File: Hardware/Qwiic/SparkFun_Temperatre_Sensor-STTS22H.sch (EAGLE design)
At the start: 28 parts, among them J1 QWIIC_RIGHT_ANGLE, J2 QWIIC_RIGHT_ANGLE, U2 STTS22H

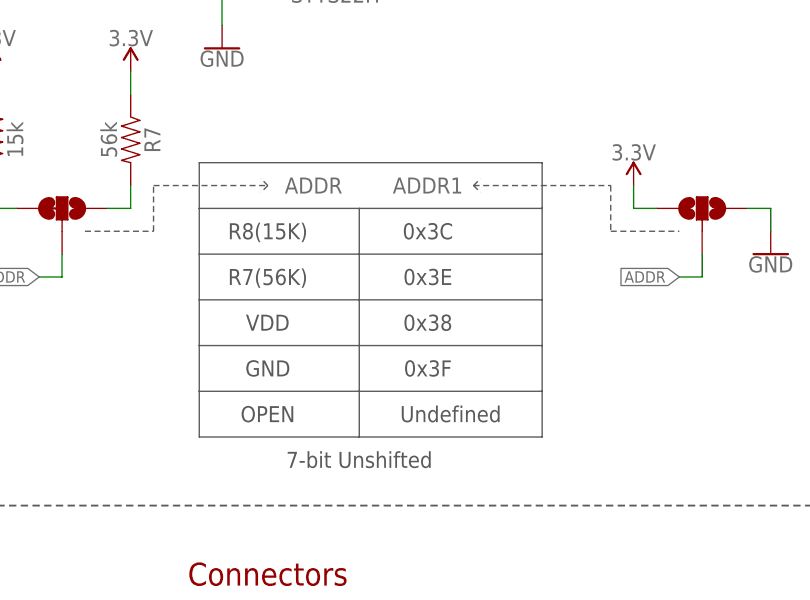
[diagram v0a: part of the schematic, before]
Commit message: Adds note for default addresses
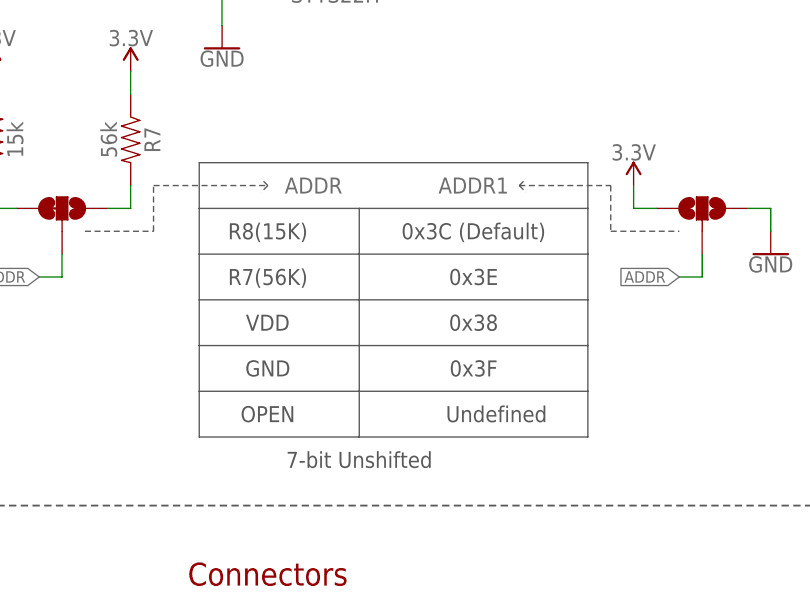
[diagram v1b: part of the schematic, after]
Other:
- note added: "0x3C (Default)"
- note removed: "0x3C"
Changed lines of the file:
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@@
 <wire x1="40.64" y1="86.36" x2="40.64" y2="81.28" width="0.1524" layer="97"/>
 <wire x1="40.64" y1="81.28" x2="40.64" y2="76.2" width="0.1524" layer="97"/>
-<wire x1="58.42" y1="76.2" x2="78.74" y2="76.2" width="0.1524" layer="97"/>
-<wire x1="78.74" y1="76.2" x2="78.74" y2="81.28" width="0.1524" layer="97"/>
-<wire x1="78.74" y1="81.28" x2="78.74" y2="86.36" width="0.1524" layer="97"/>
-<wire x1="78.74" y1="86.36" x2="78.74" y2="91.44" width="0.1524" layer="97"/>
-<wire x1="78.74" y1="91.44" x2="78.74" y2="96.52" width="0.1524" layer="97"/>
-<wire x1="78.74" y1="96.52" x2="78.74" y2="101.6" width="0.1524" layer="97"/>
-<wire x1="78.74" y1="101.6" x2="78.74" y2="106.68" width="0.1524" layer="97"/>
-<wire x1="78.74" y1="106.68" x2="40.64" y2="106.68" width="0.1524" layer="97"/>
+<wire x1="58.42" y1="76.2" x2="83.82" y2="76.2" width="0.1524" layer="97"/>
+<wire x1="83.82" y1="76.2" x2="83.82" y2="81.28" width="0.1524" layer="97"/>
+<wire x1="83.82" y1="81.28" x2="83.82" y2="86.36" width="0.1524" layer="97"/>
+<wire x1="83.82" y1="86.36" x2="83.82" y2="91.44" width="0.1524" layer="97"/>
+<wire x1="83.82" y1="91.44" x2="83.82" y2="96.52" width="0.1524" layer="97"/>
+<wire x1="83.82" y1="96.52" x2="83.82" y2="101.6" width="0.1524" layer="97"/>
+<wire x1="83.82" y1="101.6" x2="83.82" y2="106.68" width="0.1524" layer="97"/>
+<wire x1="83.82" y1="106.68" x2="40.64" y2="106.68" width="0.1524" layer="97"/>
 <wire x1="40.64" y1="101.6" x2="58.42" y2="101.6" width="0.1524" layer="97"/>
-<wire x1="58.42" y1="101.6" x2="78.74" y2="101.6" width="0.1524" layer="97"/>
+<wire x1="58.42" y1="101.6" x2="83.82" y2="101.6" width="0.1524" layer="97"/>
 <wire x1="58.42" y1="101.6" x2="58.42" y2="96.52" width="0.1524" layer="97"/>
 <wire x1="58.42" y1="96.52" x2="58.42" y2="91.44" width="0.1524" layer="97"/>
@@
 <wire x1="40.64" y1="81.28" x2="58.42" y2="81.28" width="0.1524" layer="97"/>
 <wire x1="40.64" y1="76.2" x2="58.42" y2="76.2" width="0.1524" layer="97"/>
-<wire x1="58.42" y1="96.52" x2="78.74" y2="96.52" width="0.1524" layer="97"/>
-<wire x1="58.42" y1="81.28" x2="78.74" y2="81.28" width="0.1524" layer="97"/>
+<wire x1="58.42" y1="96.52" x2="83.82" y2="96.52" width="0.1524" layer="97"/>
+<wire x1="58.42" y1="81.28" x2="83.82" y2="81.28" width="0.1524" layer="97"/>
 <text x="48.26" y="88.9" size="1.778" layer="97" font="vector" align="center">VDD</text>
 <text x="48.26" y="83.82" size="1.778" layer="97" font="vector" align="center">GND</text>
 <text x="48.26" y="78.74" size="1.778" layer="97" font="vector" align="center">OPEN</text>
-<text x="68.58" y="78.74" size="1.778" layer="97" font="vector" align="center">Undefined</text>
+<text x="73.66" y="78.74" size="1.778" layer="97" font="vector" align="center">Undefined</text>
 <text x="58.42" y="73.66" size="1.778" layer="97" font="vector" align="center">7-bit Unshifted</text>
 <wire x1="40.64" y1="91.44" x2="58.42" y2="91.44" width="0.1524" layer="97"/>
-<wire x1="58.42" y1="91.44" x2="78.74" y2="91.44" width="0.1524" layer="97"/>
+<wire x1="58.42" y1="91.44" x2="83.82" y2="91.44" width="0.1524" layer="97"/>
 <wire x1="40.64" y1="86.36" x2="58.42" y2="86.36" width="0.1524" layer="97"/>
-<wire x1="58.42" y1="86.36" x2="78.74" y2="86.36" width="0.1524" layer="97"/>
+<wire x1="58.42" y1="86.36" x2="83.82" y2="86.36" width="0.1524" layer="97"/>
 <text x="48.26" y="93.98" size="1.778" layer="97" font="vector" align="center">R7(56K)</text>
 <text x="48.26" y="99.06" size="1.778" layer="97" font="vector" align="center">R8(15K)</text>
-<text x="66.04" y="88.9" size="1.778" layer="97" font="vector" align="center">0x38</text>
-<text x="66.04" y="99.06" size="1.778" layer="97" font="vector" align="center">0x3C</text>
-<text x="66.04" y="93.98" size="1.778" layer="97" font="vector" align="center">0x3E</text>
-<text x="66.04" y="83.82" size="1.778" layer="97" font="vector" align="center">0x3F</text>
+<text x="71.12" y="88.9" size="1.778" layer="97" font="vector" align="center">0x38</text>
+<text x="71.12" y="99.06" size="1.778" layer="97" font="vector" align="center">0x3C (Default)</text>
+<text x="71.12" y="93.98" size="1.778" layer="97" font="vector" align="center">0x3E</text>
+<text x="71.12" y="83.82" size="1.778" layer="97" font="vector" align="center">0x3F</text>
 <wire x1="27.94" y1="99.06" x2="35.56" y2="99.06" width="0.1524" layer="97" style="dashdot"/>
 <wire x1="35.56" y1="99.06" x2="35.56" y2="104.14" width="0.1524" layer="97" style="dashdot"/>
 <wire x1="35.56" y1="104.14" x2="48.26" y2="104.14" width="0.1524" layer="97" style="dashdot"/>
-<wire x1="71.12" y1="104.14" x2="86.36" y2="104.14" width="0.1524" layer="97" style="dashdot"/>
+<wire x1="76.2" y1="104.14" x2="86.36" y2="104.14" width="0.1524" layer="97" style="dashdot"/>
 <wire x1="86.36" y1="104.14" x2="86.36" y2="99.06" width="0.1524" layer="97" style="dashdot"/>
 <wire x1="86.36" y1="99.06" x2="93.98" y2="99.06" width="0.1524" layer="97" style="dashdot"/>
 <wire x1="48.26" y1="104.14" x2="47.498" y2="104.902" width="0.1524" layer="97" style="dashdot"/>
 <wire x1="48.26" y1="104.14" x2="47.498" y2="103.378" width="0.1524" layer="97" style="dashdot"/>
-<wire x1="71.12" y1="104.14" x2="71.882" y2="104.902" width="0.1524" layer="97" style="dashdot"/>
-<wire x1="71.12" y1="104.14" x2="71.882" y2="103.378" width="0.1524" layer="97" style="dashdot"/>
+<wire x1="76.2" y1="104.14" x2="76.962" y2="104.902" width="0.1524" layer="97" style="dashdot"/>
+<wire x1="76.2" y1="104.14" x2="76.962" y2="103.378" width="0.1524" layer="97" style="dashdot"/>
 <text x="58.42" y="175.26" size="2.54" layer="94" font="vector" align="center">Temperature Sensor - STTS22H</text>
 </plain>
@@
 </instance>
 <instance part="ADDR1" gate="G$1" x="96.52" y="101.6" smashed="yes" rot="MR90">
-<attribute name="NAME" x="66.04" y="104.14" size="1.778" layer="95" font="vector" rot="MR0" align="center"/>
+<attribute name="NAME" x="71.12" y="104.14" size="1.778" layer="95" font="vector" rot="MR0" align="center"/>
 </instance>
 <instance part="SUPPLY8" gate="G$1" x="88.9" y="104.14" smashed="yes">

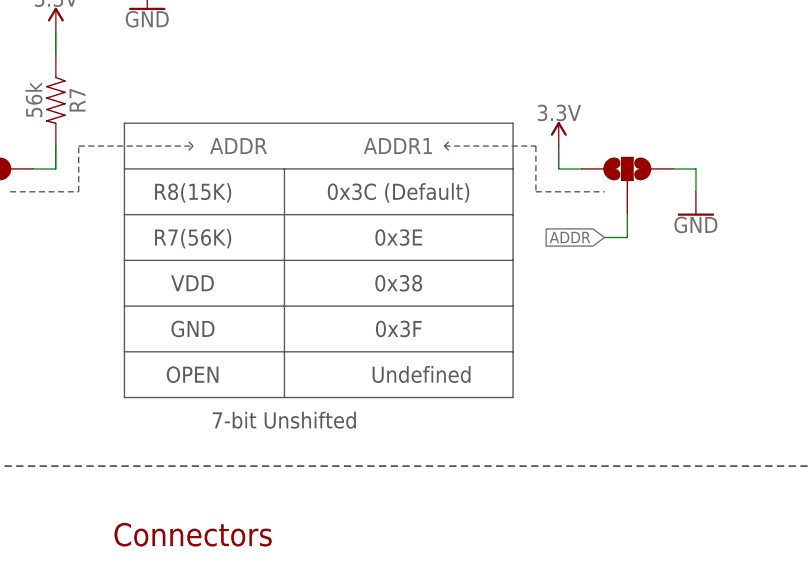
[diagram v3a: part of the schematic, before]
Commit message: Updates temp sensor footprint, Adds bstop underneath IC
* Adds via directly underneath sensor for better temperature sensing
* Fixes various routing inconsistencies
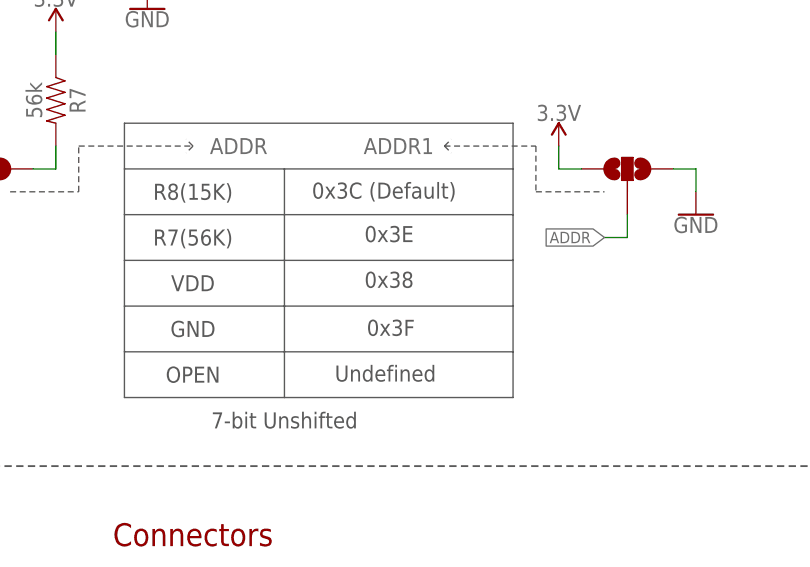
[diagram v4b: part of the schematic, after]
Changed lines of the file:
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@@
 <text x="48.26" y="83.82" size="1.778" layer="97" font="vector" align="center">GND</text>
 <text x="48.26" y="78.74" size="1.778" layer="97" font="vector" align="center">OPEN</text>
-<text x="73.66" y="78.74" size="1.778" layer="97" font="vector" align="center">Undefined</text>
+<text x="64.008" y="77.978" size="1.778" layer="97" font="vector">Undefined</text>
 <text x="58.42" y="73.66" size="1.778" layer="97" font="vector" align="center">7-bit Unshifted</text>
 <wire x1="40.64" y1="91.44" x2="58.42" y2="91.44" width="0.1524" layer="97"/>
@@
 <text x="48.26" y="93.98" size="1.778" layer="97" font="vector" align="center">R7(56K)</text>
 <text x="48.26" y="99.06" size="1.778" layer="97" font="vector" align="center">R8(15K)</text>
-<text x="71.12" y="88.9" size="1.778" layer="97" font="vector" align="center">0x38</text>
-<text x="71.12" y="99.06" size="1.778" layer="97" font="vector" align="center">0x3C (Default)</text>
-<text x="71.12" y="93.98" size="1.778" layer="97" font="vector" align="center">0x3E</text>
-<text x="71.12" y="83.82" size="1.778" layer="97" font="vector" align="center">0x3F</text>
+<text x="67.31" y="88.392" size="1.778" layer="97" font="vector">0x38</text>
+<text x="61.468" y="98.298" size="1.778" layer="97" font="vector" ratio="15">0x3C (Default)</text>
+<text x="67.31" y="93.472" size="1.778" layer="97" font="vector">0x3E</text>
+<text x="67.564" y="83.058" size="1.778" layer="97" font="vector">0x3F</text>
 <wire x1="27.94" y1="99.06" x2="35.56" y2="99.06" width="0.1524" layer="97" style="dashdot"/>
 <wire x1="35.56" y1="99.06" x2="35.56" y2="104.14" width="0.1524" layer="97" style="dashdot"/>

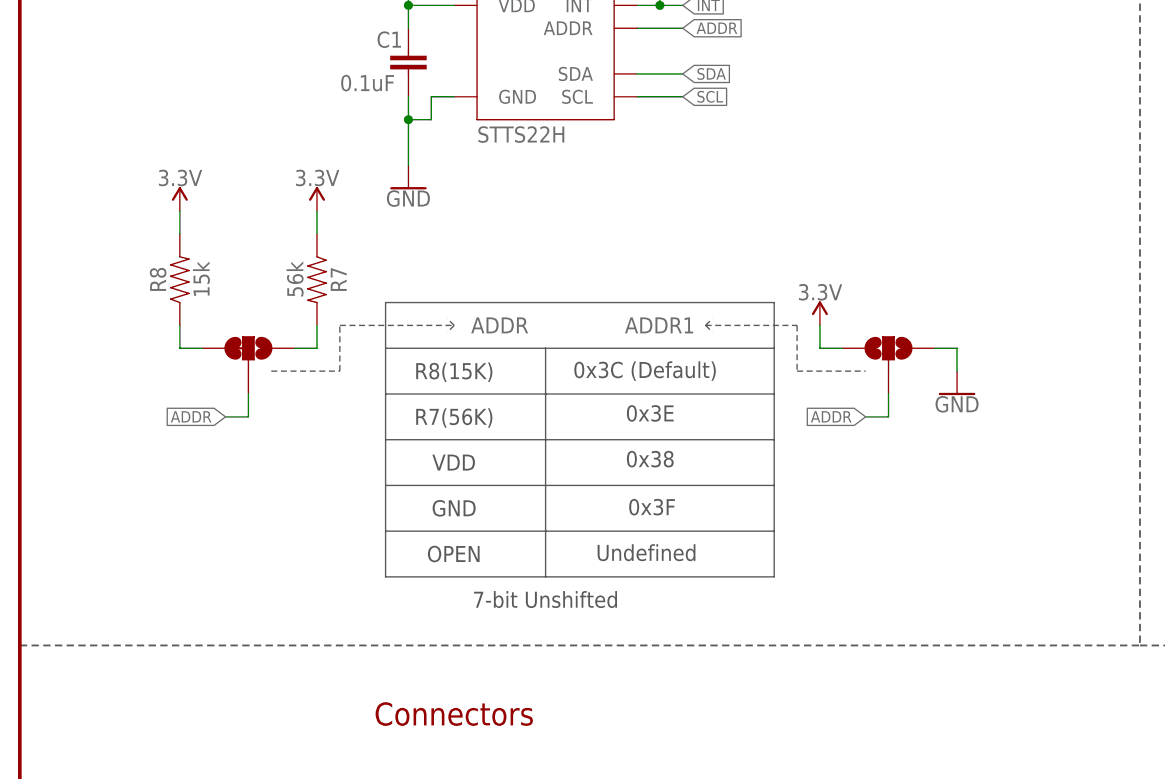
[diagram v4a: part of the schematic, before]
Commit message: Moves address selection around to be more clear in the schematic
* Changes second address option on micro to 3v3 instead of GND
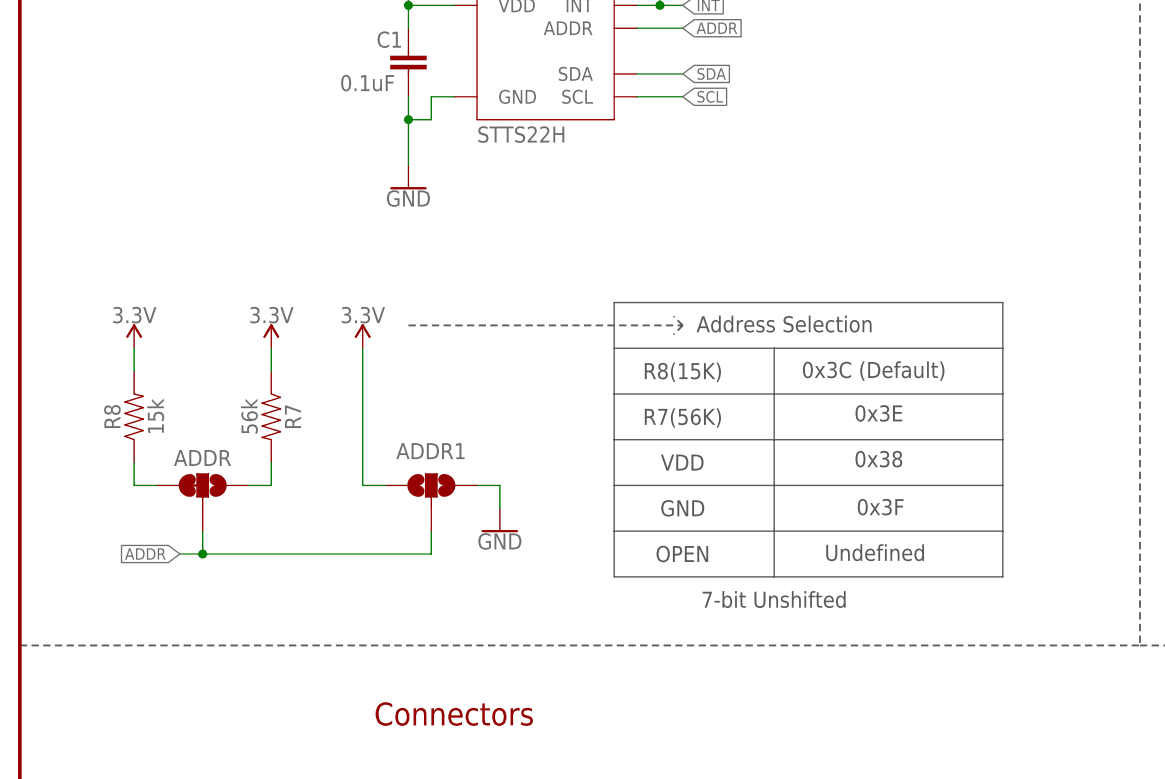
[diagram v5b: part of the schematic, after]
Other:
- note added: "Address Selection"
- moved on the sheet: ADDR, ADDR1, R7, R8
